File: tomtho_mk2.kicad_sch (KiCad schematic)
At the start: 173 parts, among them J1 USB-C, J2 BATTERY, J3 TRACKPAD, Q1 AO3401A, SW1 SKRAAWE010, SW10 SKRAAWE010, SW11 SKRAAWE010, SW12 SKRAAWE010, SW13 SKRAAWE010, SW14 SKRAAWE010, SW15 SKRAAWE010, SW16 SKRAAWE010, SW17 SKRAAWE010, SW18 SKRAAWE010, SW19 SKRAAWE010, SW2 SKRAAWE010, SW20 SKRAAWE010, SW21 SKRAAWE010, SW22 SKRAAWE010, SW23 SKRAAWE010, SW24 SKRAAWE010, SW25 SKRAAWE010, SW26 SKRAAWE010, SW27 SKRAAWE010, SW28 SKRAAWE010, SW29 SKRAAWE010, SW3 SKRAAWE010, SW30 SKRAAWE010, SW31 SKRAAWE010, SW32 SKRAAWE010, SW33 SKRAAWE010, SW34 SKRAAWE010, SW35 SKRAAWE010, SW36 SKRAAWE010, SW37 SKRAAWE010, SW38 SKRAAWE010, SW39 SKRAAWE010, SW4 SKRAAWE010, SW40 SKRAAWE010, SW41 SKRAAWE010, SW42 SKRAAWE010, SW43 SKRAAWE010, SW44 SKRAAWE010, SW45 SKRAAWE010, SW46 SKRAAWE010, SW47 SKRAAWE010, SW48 SKRAAWE010, SW49 SKRAAWE010, SW5 SKRAAWE010, SW50 SKRAAWE010, SW51 SKRAAWE010, SW52 SKRAAWE010, SW53 SKRAAWE010, SW54 SKRAAWE010, SW55 SKRAAWE010, SW56 SKRAAWE010, SW57 SKRAAWE010, SW58 SKRAAWE010, SW59 SKRAAWE010, SW6 SKRAAWE010, SW60 SKRAAWE010, SW61 SKRAAWE010, SW62 SKRAAWE010, SW63 SKRAAWE010, SW64 SKRAAWE010, SW65 SKRAAWE010, SW66 RESET, SW67 POWER, SW7 SKRAAWE010, SW8 SKRAAWE010, SW9 SKRAAWE010, U1 MDBT50Q-1MV2, U2 USBLC6-2SC6, U3 MCP73831

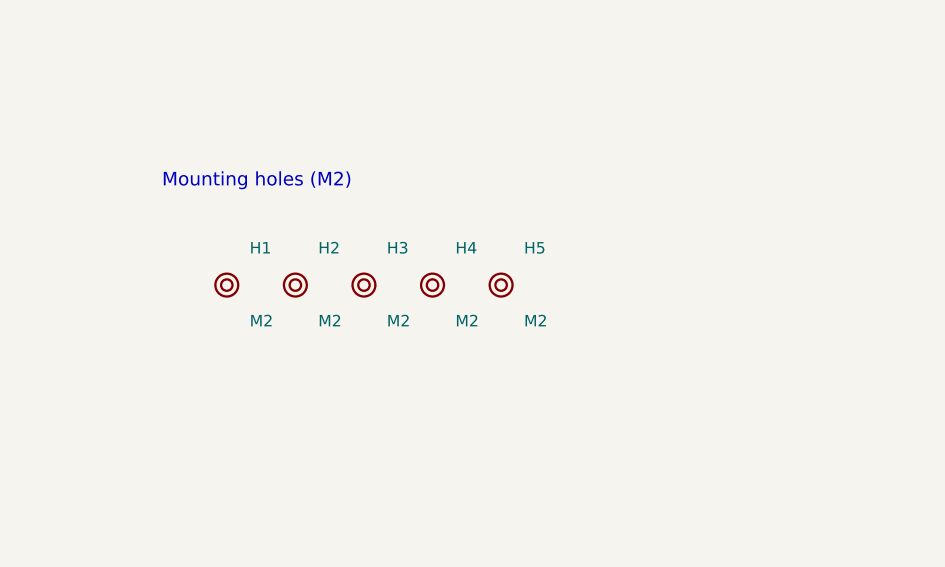
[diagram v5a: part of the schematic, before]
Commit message: mk2: case v1 (top frame + bottom plate + 0.5u x 0.5u flange cap) in CadQuery; PCB: 11 case screws in rear strip / front edge, arrow diodes and J3 moved clear of ACC keycap legs, USB D- bridge protected; DRC 0/0/0
Co-Authored-By: Claude Opus 5.5 <noreply@anthropic.com>
Claude-Session: https://claude.ai/code/session_014QKLhpB6tKWk1p8Y7v384p
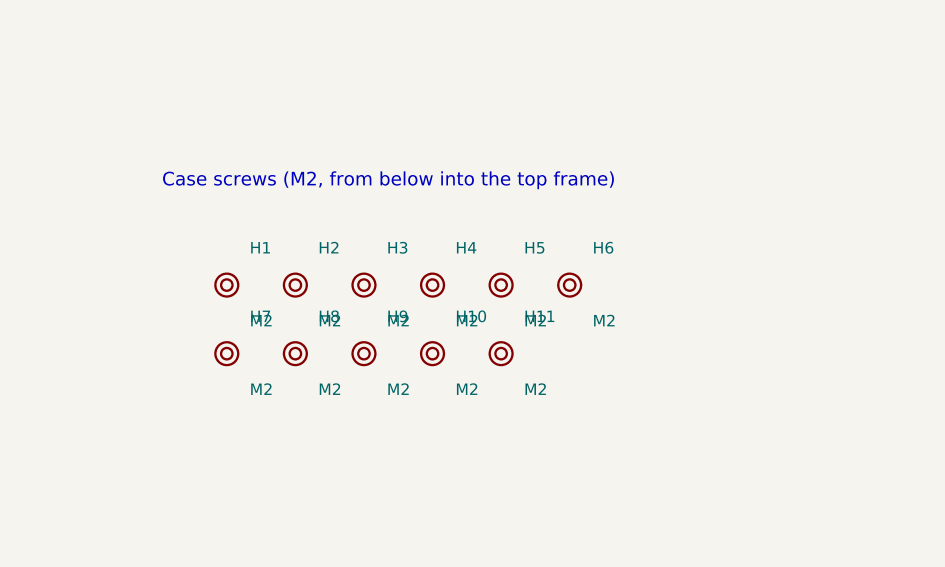
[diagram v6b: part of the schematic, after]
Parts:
- added H10, H11, H6, H7, H8, H9: M2, tomtho_mk2:MountingHole_2.2mm_M2, symbol tomtho_mk2:MountingHole
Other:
- note added: "Case screws (M2, from below into the top frame)"
- note removed: "Mounting holes (M2)"
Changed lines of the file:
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@@
 	(label "VDD" (at 518.16 100.33 90) (effects (font (size 1.27 1.27)) (justify left bottom)))
 	(label "TP_SCL" (at 518.16 107.95 270) (effects (font (size 1.27 1.27)) (justify right bottom)))
-	(text "Mounting holes (M2)" (exclude_from_sim no) (at 450 140 0) (effects (font (size 1.5 1.5)) (justify left top)))
+	(text "Case screws (M2, from below into the top frame)" (exclude_from_sim no) (at 450 140 0) (effects (font (size 1.5 1.5)) (justify left top)))
 	(symbol (lib_id "tomtho_mk2:MountingHole") (at 457.2 152.4 0) (unit 1) (exclude_from_sim no) (in_bom no) (on_board yes) (dnp no)
 		(property "Reference" "H1" (at 459.74 148.3 0) (effects (font (size 1.27 1.27)) (justify left)))
@@
 		(instances (project "tomtho_mk2" (path "/cb8fbeca-ed00-5759-aba1-2394e5039438" (reference "H5") (unit 1))))
 	)
+	(symbol (lib_id "tomtho_mk2:MountingHole") (at 495.3 152.4 0) (unit 1) (exclude_from_sim no) (in_bom no) (on_board yes) (dnp no)
+		(property "Reference" "H6" (at 497.84 148.3 0) (effects (font (size 1.27 1.27)) (justify left)))
+		(property "Value" "M2" (at 497.84 156.4 0) (effects (font (size 1.27 1.27)) (justify left)))
+		(property "Footprint" "tomtho_mk2:MountingHole_2.2mm_M2" (at 495.3 152.4 0) (effects (font (size 1.27 1.27)) (hide yes)))
+		(property "Datasheet" "~" (at 495.3 152.4 0) (effects (font (size 1.27 1.27)) (hide yes)))
+		(property "Description" "" (at 495.3 152.4 0) (effects (font (size 1.27 1.27)) (hide yes)))
+		(property "LCSC" "" (at 495.3 152.4 0) (effects (font (size 1.27 1.27)) (hide yes)))
+		(property "MPN" "" (at 495.3 152.4 0) (effects (font (size 1.27 1.27)) (hide yes)))
+		(instances (project "tomtho_mk2" (path "/cb8fbeca-ed00-5759-aba1-2394e5039438" (reference "H6") (unit 1))))
+	)
+	(symbol (lib_id "tomtho_mk2:MountingHole") (at 457.2 160.02 0) (unit 1) (exclude_from_sim no) (in_bom no) (on_board yes) (dnp no)
+		(property "Reference" "H7" (at 459.74 155.92 0) (effects (font (size 1.27 1.27)) (justify left)))
+		(property "Value" "M2" (at 459.74 164.02 0) (effects (font (size 1.27 1.27)) (justify left)))
+		(property "Footprint" "tomtho_mk2:MountingHole_2.2mm_M2" (at 457.2 160.02 0) (effects (font (size 1.27 1.27)) (hide yes)))
+		(property "Datasheet" "~" (at 457.2 160.02 0) (effects (font (size 1.27 1.27)) (hide yes)))
+		(property "Description" "" (at 457.2 160.02 0) (effects (font (size 1.27 1.27)) (hide yes)))
+		(property "LCSC" "" (at 457.2 160.02 0) (effects (font (size 1.27 1.27)) (hide yes)))
+		(property "MPN" "" (at 457.2 160.02 0) (effects (font (size 1.27 1.27)) (hide yes)))
+		(instances (project "tomtho_mk2" (path "/cb8fbeca-ed00-5759-aba1-2394e5039438" (reference "H7") (unit 1))))
+	)
+	(symbol (lib_id "tomtho_mk2:MountingHole") (at 464.82 160.02 0) (unit 1) (exclude_from_sim no) (in_bom no) (on_board yes) (dnp no)
+		(property "Reference" "H8" (at 467.36 155.92 0) (effects (font (size 1.27 1.27)) (justify left)))
+		(property "Value" "M2" (at 467.36 164.02 0) (effects (font (size 1.27 1.27)) (justify left)))
+		(property "Footprint" "tomtho_mk2:MountingHole_2.2mm_M2" (at 464.82 160.02 0) (effects (font (size 1.27 1.27)) (hide yes)))
+		(property "Datasheet" "~" (at 464.82 160.02 0) (effects (font (size 1.27 1.27)) (hide yes)))
+		(property "Description" "" (at 464.82 160.02 0) (effects (font (size 1.27 1.27)) (hide yes)))
+		(property "LCSC" "" (at 464.82 160.02 0) (effects (font (size 1.27 1.27)) (hide yes)))
+		(property "MPN" "" (at 464.82 160.02 0) (effects (font (size 1.27 1.27)) (hide yes)))
+		(instances (project "tomtho_mk2" (path "/cb8fbeca-ed00-5759-aba1-2394e5039438" (reference "H8") (unit 1))))
+	)
+	(symbol (lib_id "tomtho_mk2:MountingHole") (at 472.44 160.02 0) (unit 1) (exclude_from_sim no) (in_bom no) (on_board yes) (dnp no)
+		(property "Reference" "H9" (at 474.98 155.92 0) (effects (font (size 1.27 1.27)) (justify left)))
+		(property "Value" "M2" (at 474.98 164.02 0) (effects (font (size 1.27 1.27)) (justify left)))
+		(property "Footprint" "tomtho_mk2:MountingHole_2.2mm_M2" (at 472.44 160.02 0) (effects (font (size 1.27 1.27)) (hide yes)))
+		(property "Datasheet" "~" (at 472.44 160.02 0) (effects (font (size 1.27 1.27)) (hide yes)))
+		(property "Description" "" (at 472.44 160.02 0) (effects (font (size 1.27 1.27)) (hide yes)))
+		(property "LCSC" "" (at 472.44 160.02 0) (effects (font (size 1.27 1.27)) (hide yes)))
+		(property "MPN" "" (at 472.44 160.02 0) (effects (font (size 1.27 1.27)) (hide yes)))
+		(instances (project "tomtho_mk2" (path "/cb8fbeca-ed00-5759-aba1-2394e5039438" (reference "H9") (unit 1))))
+	)
+	(symbol (lib_id "tomtho_mk2:MountingHole") (at 480.06 160.02 0) (unit 1) (exclude_from_sim no) (in_bom no) (on_board yes) (dnp no)
+		(property "Reference" "H10" (at 482.6 155.92 0) (effects (font (size 1.27 1.27)) (justify left)))
+		(property "Value" "M2" (at 482.6 164.02 0) (effects (font (size 1.27 1.27)) (justify left)))
+		(property "Footprint" "tomtho_mk2:MountingHole_2.2mm_M2" (at 480.06 160.02 0) (effects (font (size 1.27 1.27)) (hide yes)))
+		(property "Datasheet" "~" (at 480.06 160.02 0) (effects (font (size 1.27 1.27)) (hide yes)))
+		(property "Description" "" (at 480.06 160.02 0) (effects (font (size 1.27 1.27)) (hide yes)))
+		(property "LCSC" "" (at 480.06 160.02 0) (effects (font (size 1.27 1.27)) (hide yes)))
+		(property "MPN" "" (at 480.06 160.02 0) (effects (font (size 1.27 1.27)) (hide yes)))
+		(instances (project "tomtho_mk2" (path "/cb8fbeca-ed00-5759-aba1-2394e5039438" (reference "H10") (unit 1))))
+	)
+	(symbol (lib_id "tomtho_mk2:MountingHole") (at 487.68 160.02 0) (unit 1) (exclude_from_sim no) (in_bom no) (on_board yes) (dnp no)
+		(property "Reference" "H11" (at 490.22 155.92 0) (effects (font (size 1.27 1.27)) (justify left)))
+		(property "Value" "M2" (at 490.22 164.02 0) (effects (font (size 1.27 1.27)) (justify left)))
+		(property "Footprint" "tomtho_mk2:MountingHole_2.2mm_M2" (at 487.68 160.02 0) (effects (font (size 1.27 1.27)) (hide yes)))
+		(property "Datasheet" "~" (at 487.68 160.02 0) (effects (font (size 1.27 1.27)) (hide yes)))
+		(property "Description" "" (at 487.68 160.02 0) (effects (font (size 1.27 1.27)) (hide yes)))
+		(property "LCSC" "" (at 487.68 160.02 0) (effects (font (size 1.27 1.27)) (hide yes)))
+		(property "MPN" "" (at 487.68 160.02 0) (effects (font (size 1.27 1.27)) (hide yes)))
+		(instances (project "tomtho_mk2" (path "/cb8fbeca-ed00-5759-aba1-2394e5039438" (reference "H11") (unit 1))))
+	)
 	(text "GPIO map (ZMK, diode-direction = col2row)\nrows:  ROW0=P1.10, ROW1=P1.11, ROW2=P1.13, ROW3=P1.15, ROW4=P0.29/AIN5, ROW5=P0.31/AIN7\ncols:  COL0=P0.30/AIN6, COL1=P0.27, COL2=P0.04/AIN2, COL3=P0.06, COL4=P0.08, COL5=P1.09\n       COL6=P0.24, COL7=P0.22, COL8=P0.20, COL9=P0.17, COL10=P0.15, COL11=P0.13\nLED (active low): LED_BT1=P1.12, LED_BT2=P1.14, LED_BT3=P0.03/AIN1, LED_PWR_G=P0.02/AIN0, LED_PWR_R=P0.28/AIN4\ntrackpad: TP_SDA=P0.14, TP_SCL=P0.16, TP_RDY=P0.19, TP_RST=P0.21" (exclude_from_sim no) (at 150 128 0) (effects (font (size 1.27 1.27)) (justify left top)))

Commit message: Ashiyu: name in KiCad title blocks, READMEs and ORDER (DRC 0/0/0, parity 0)
Co-Authored-By: Claude Opus 5.5 <noreply@anthropic.com>
Claude-Session: https://claude.ai/code/session_014QKLhpB6tKWk1p8Y7v384p
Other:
- title: tomtho-slim mk2 -> Ashiyu (tomtho-slim mk2)
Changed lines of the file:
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@@
 	(paper "A2")
 	(title_block
-		(title "tomtho-slim mk2")
+		(title "Ashiyu (tomtho-slim mk2)")
 		(date "2026-10-07")
 		(rev "mk2-0.1")

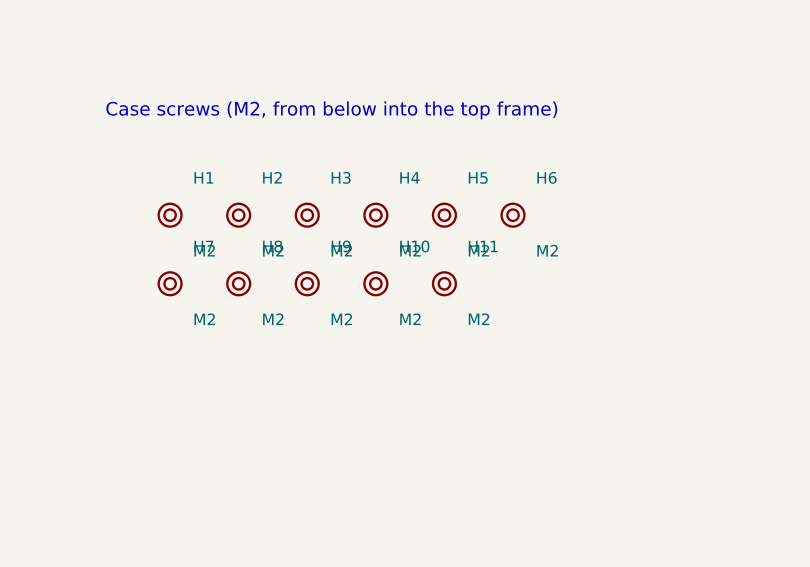
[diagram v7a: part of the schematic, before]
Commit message: Ashiyu: screwless case - skirt down to the desk, bottom tray inside with 8 hidden spring clips; PCB floats on 8 Tadpole D3.0 pins (4 rear, 2 front, 2 centre); PCB holes d3.1 (DRC 0/0/0)
Co-Authored-By: Claude Opus 5.5 <noreply@anthropic.com>
Claude-Session: https://claude.ai/code/session_014QKLhpB6tKWk1p8Y7v384p
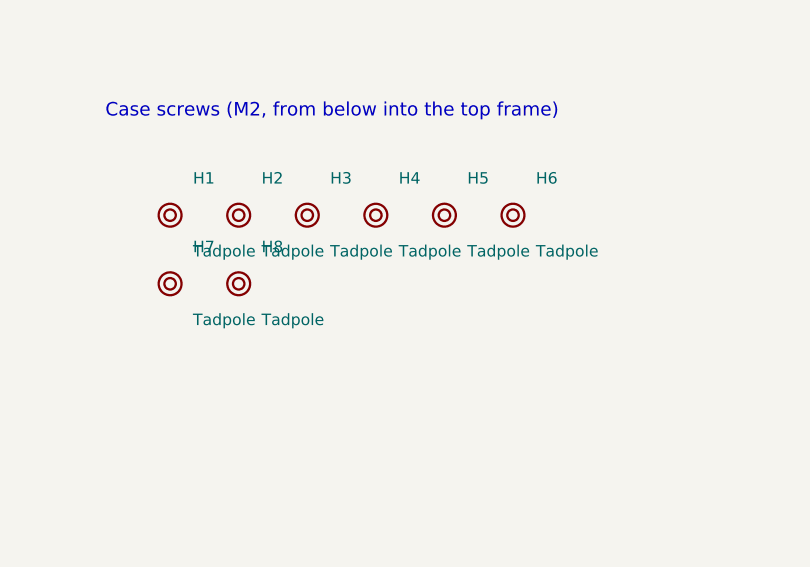
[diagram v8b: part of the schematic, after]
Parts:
- removed H10, H11, H9: M2, tomtho_mk2:MountingHole_2.2mm_M2, symbol tomtho_mk2:MountingHole
- H1, H2, H3, H4, H5, H6, H7, H8: value M2 -> Tadpole; footprint tomtho_mk2:MountingHole_2.2mm_M2 -> tomtho_mk2:Tadpole_D3.0_NPTH
